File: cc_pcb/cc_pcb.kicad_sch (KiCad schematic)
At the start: 70 parts, among them J1 Conn_02x05_Odd_Even, J10 AC-DC Converter, J2 Wi-Fi Module, J3 Controller (40Pin->SPI), J4 RFID Scanner, J5 4x4 Keypad, J6 SD Reader, J7 PS_Modules, J8 PS_Designed, J9 DC-DC Converter, SW1 SW_Push, U1 STM32F091RCTx, U2 LM393, U3 LD1117S33TR_SOT223

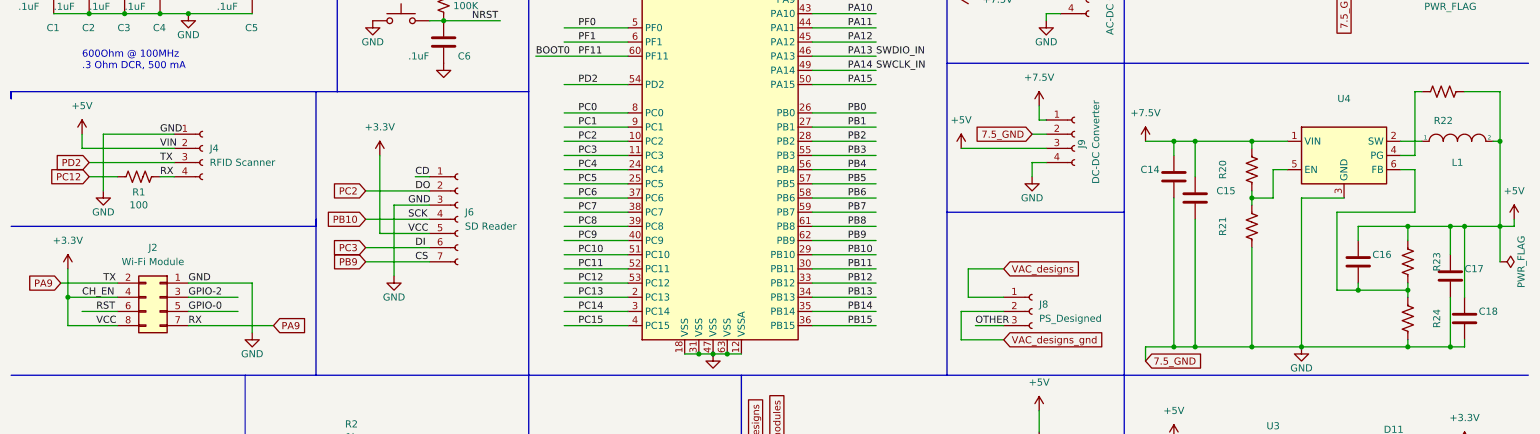
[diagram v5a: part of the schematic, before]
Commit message: RA8875 and ESP8266 updated footprints
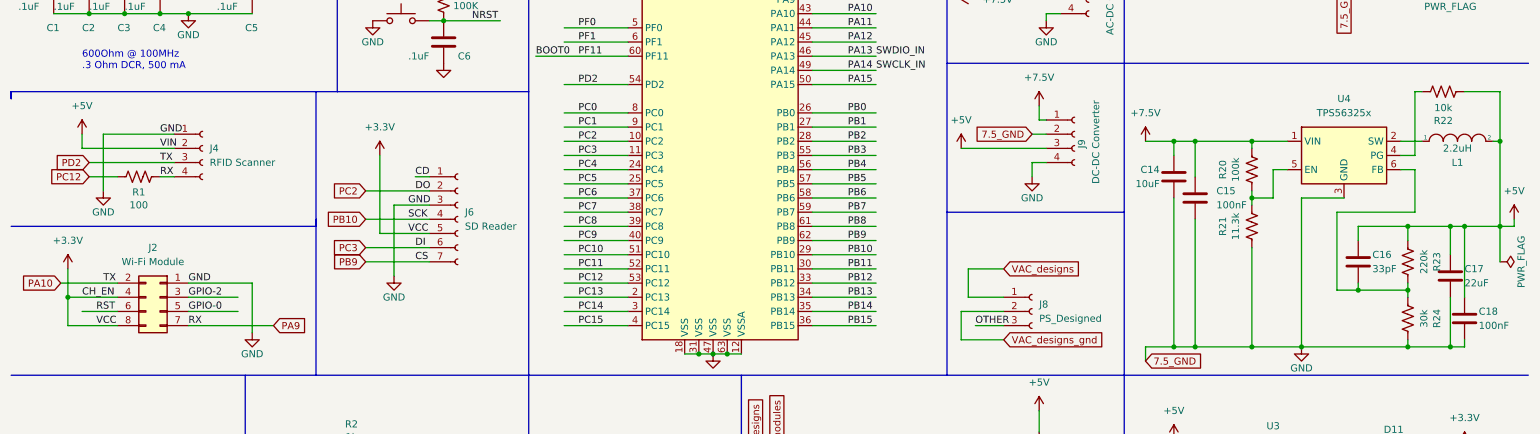
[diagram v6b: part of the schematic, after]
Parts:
- C14: value (none) -> 10uF
- C15, C18: value (none) -> 100nF
- C16: value (none) -> 33pF
- C17: value (none) -> 22uF
- L1: value (none) -> 2.2uH
- R20: value (none) -> 100k
- R21: value (none) -> 11.3k
- R22: value (none) -> 10k
- R23: value (none) -> 220k
- R24: value (none) -> 30k
- U4: value (none) -> TPS56325x
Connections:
- net PA10: now also J2.2 (Pin_2), J4.3 (Pin_3), U1.54 (PD2)
- net PA9: no longer J2.2 (Pin_2), J4.3 (Pin_3), U1.54 (PD2)
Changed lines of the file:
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@@
     )
   )
-  (global_label "PA9" (shape input) (at 21.59 105.41 180) (fields_autoplaced)
+  (global_label "PA10" (shape input) (at 21.59 105.41 180) (fields_autoplaced)
     (effects (font (size 1.27 1.27)) (justify right))
-    (property "Intersheet References" "${INTERSHEET_REFS}" (id 0) (at 15.6088 105.3306 0)
+    (property "Intersheet References" "${INTERSHEET_REFS}" (id 0) (at 14.3993 105.3306 0)
       (effects (font (size 1.27 1.27)) (justify right) hide)
     )
@@
     (in_bom yes) (on_board yes)
     (property "Reference" "R22" (id 0) (at 269.24 76.327 90))
-    (property "Value" "" (id 1) (at 269.24 74.0156 90))
+    (property "Value" "10k" (id 1) (at 269.24 74.0156 90))
     (property "Footprint" "Resistor_SMD:R_0805_2012Metric_Pad1.20x1.40mm_HandSolder" (id 2) (at 269.494 70.104 90)
       (effects (font (size 1.27 1.27)) hide)
@@
     (in_bom yes) (on_board yes)
     (property "Reference" "R24" (id 0) (at 268.097 111.76 90))
-    (property "Value" "" (id 1) (at 265.7856 111.76 90))
+    (property "Value" "30k" (id 1) (at 265.7856 111.76 90))
     (property "Footprint" "Resistor_SMD:R_0805_2012Metric_Pad1.20x1.40mm_HandSolder" (id 2) (at 261.874 111.506 90)
       (effects (font (size 1.27 1.27)) hide)
@@
     (in_bom yes) (on_board yes)
     (property "Reference" "L1" (id 0) (at 271.78 83.82 0))
-    (property "Value" "" (id 1) (at 271.78 81.28 0))
+    (property "Value" "2.2uH" (id 1) (at 271.78 81.28 0))
     (property "Footprint" "Inductor_THT:L_Radial_D7.5mm_P5.00mm_Fastron_07P" (id 2) (at 271.78 80.01 0)
       (effects (font (size 1.27 1.27)) hide)
@@
       (effects (font (size 1.27 1.27)) (justify left))
     )
-    (property "Value" "" (id 1) (at 275.59 113.03 0)
+    (property "Value" "100nF" (id 1) (at 275.59 113.03 0)
       (effects (font (size 1.27 1.27)) (justify left))
     )
@@
     (in_bom yes) (on_board yes)
     (property "Reference" "R21" (id 0) (at 229.743 95.25 90))
-    (property "Value" "" (id 1) (at 232.0544 95.25 90))
+    (property "Value" "11.3k" (id 1) (at 232.0544 95.25 90))
     (property "Footprint" "Resistor_SMD:R_0805_2012Metric_Pad1.20x1.40mm_HandSolder" (id 2) (at 235.966 95.504 90)
       (effects (font (size 1.27 1.27)) hide)
@@
     (in_bom yes) (on_board yes)
     (property "Reference" "R23" (id 0) (at 268.097 101.6 90))
-    (property "Value" "" (id 1) (at 265.7856 101.6 90))
+    (property "Value" "220k" (id 1) (at 265.7856 101.6 90))
     (property "Footprint" "Resistor_SMD:R_0805_2012Metric_Pad1.20x1.40mm_HandSolder" (id 2) (at 261.874 101.346 90)
       (effects (font (size 1.27 1.27)) hide)
@@
       (effects (font (size 1.27 1.27)) (justify left))
     )
-    (property "Value" "" (id 1) (at 228.6 91.44 0)
+    (property "Value" "100nF" (id 1) (at 228.6 91.44 0)
       (effects (font (size 1.27 1.27)) (justify left))
     )
@@
       (effects (font (size 1.27 1.27)) (justify left))
     )
-    (property "Value" "" (id 1) (at 218.44 87.63 0)
+    (property "Value" "10uF" (id 1) (at 218.44 87.63 0)
       (effects (font (size 1.27 1.27)) (justify left))
     )
@@
     (in_bom yes) (on_board yes)
     (property "Reference" "R20" (id 0) (at 229.743 85.09 90))
-    (property "Value" "" (id 1) (at 232.0544 85.09 90))
+    (property "Value" "100k" (id 1) (at 232.0544 85.09 90))
     (property "Footprint" "Resistor_SMD:R_0805_2012Metric_Pad1.20x1.40mm_HandSolder" (id 2) (at 235.966 85.344 90)
       (effects (font (size 1.27 1.27)) hide)
@@
       (effects (font (size 1.27 1.27)) (justify left))
     )
-    (property "Value" "" (id 1) (at 256.54 102.87 0)
+    (property "Value" "33pF" (id 1) (at 256.54 102.87 0)
       (effects (font (size 1.27 1.27)) (justify left))
     )
@@
       (effects (font (size 1.27 1.27)) (justify left))
     )
-    (property "Value" "" (id 1) (at 273.05 105.41 0)
+    (property "Value" "22uF" (id 1) (at 273.05 105.41 0)
       (effects (font (size 1.27 1.27)) (justify left))
     )
@@
     (in_bom yes) (on_board yes) (fields_autoplaced)
     (property "Reference" "U4" (id 0) (at 251.46 72.39 0))
-    (property "Value" "" (id 1) (at 251.46 74.93 0))
+    (property "Value" "TPS56325x" (id 1) (at 251.46 74.93 0))
     (property "Footprint" "" (id 2) (at 252.73 88.9 0)
       (effects (font (size 1.27 1.27)) (justify left) hide)

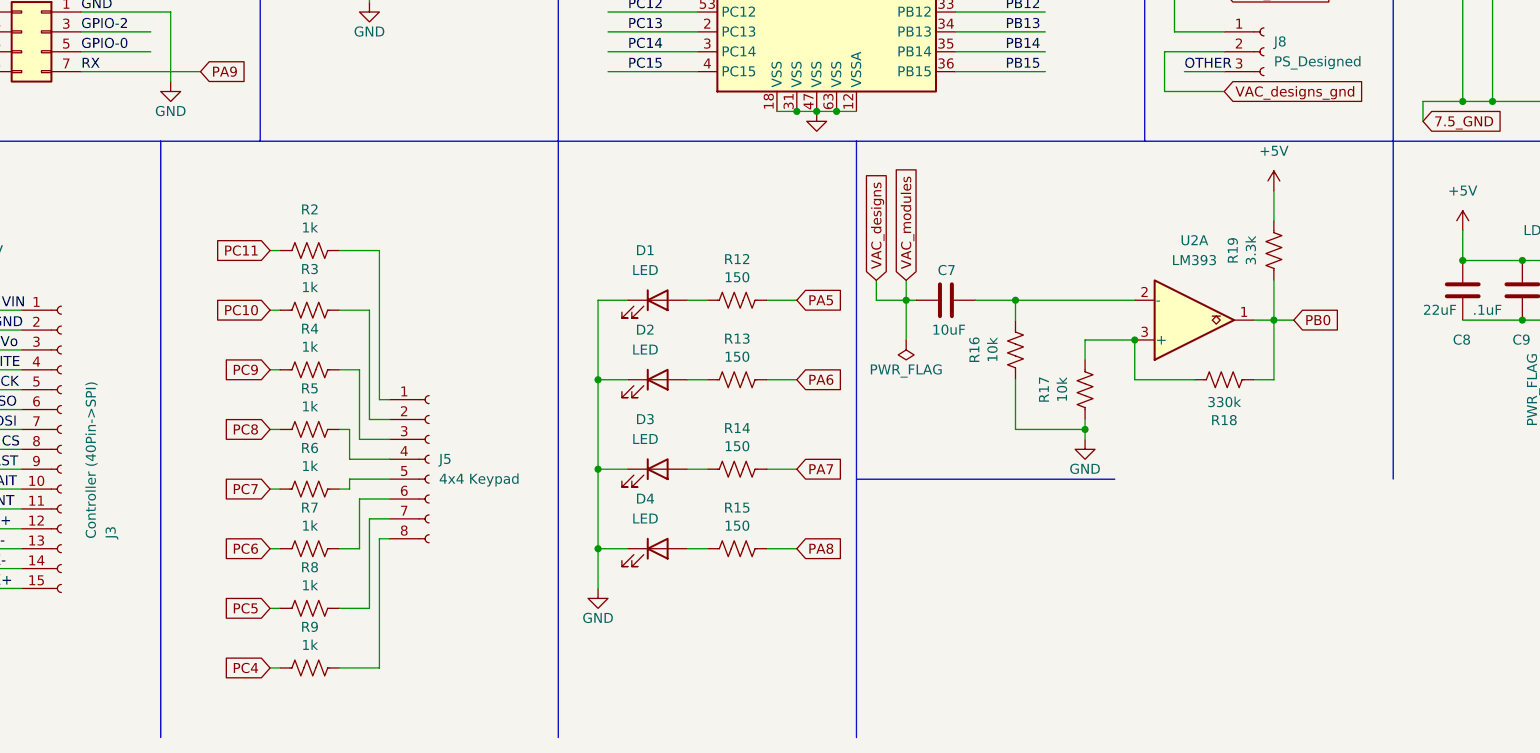
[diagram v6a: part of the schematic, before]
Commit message: added 2.8in tft display in addition to 7in one
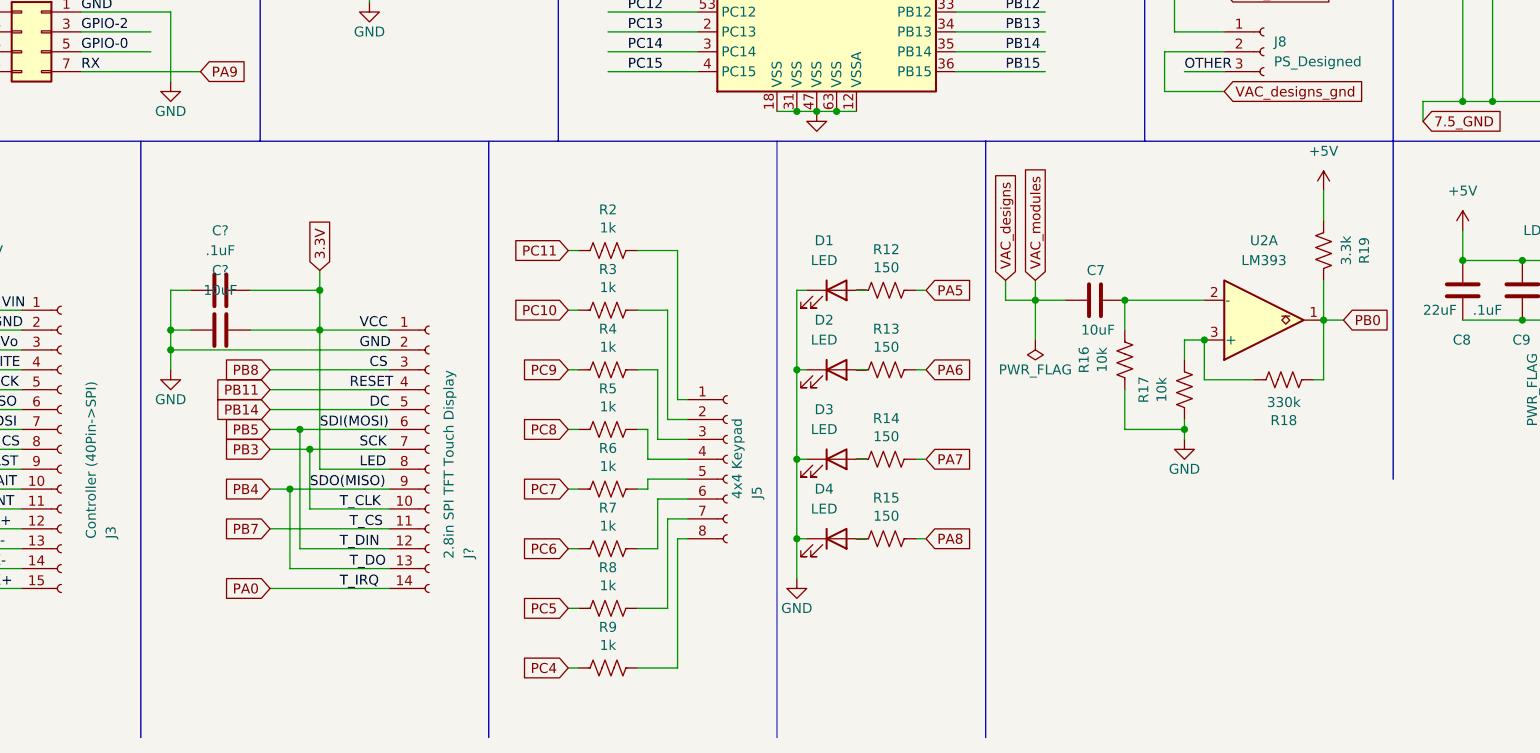
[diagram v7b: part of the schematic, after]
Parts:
- added C?: 10uF, symbol Device:C
- added C?: .1uF, symbol Device:C
- added J?: 2.8in SPI TFT Touch Display, symbol Connector:Conn_01x14_Female
- U4: footprint (none) -> imported_footprints:TPS56325x
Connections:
- net PB4 is gone; now on net PB10: J3.6 (Pin_6), U1.56 (PB4)
- net PB5 is gone; now on net +3V3: J3.7 (Pin_7), U1.57 (PB5)
- net +3V3: now also C?.2, C?.2, J?.1 (Pin_1), J?.12 (Pin_12), J?.6 (Pin_6), J?.8 (Pin_8)
- net GND: now also C?.1, C?.1, J?.2 (Pin_2)
- net PA0: now also J?.14 (Pin_14)
- net PB10: now also J?.10 (Pin_10), J?.13 (Pin_13), J?.7 (Pin_7), J?.9 (Pin_9)
- net PB11: now also J?.4 (Pin_4)
- net PB14: now also J?.5 (Pin_5)
- net PB7: now also J?.11 (Pin_11)
- net PB8: now also J?.3 (Pin_3)
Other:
- moved on the sheet: C7, D1, D2, D3, D4, J5, R12, R13, R14, R15, R16, R17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

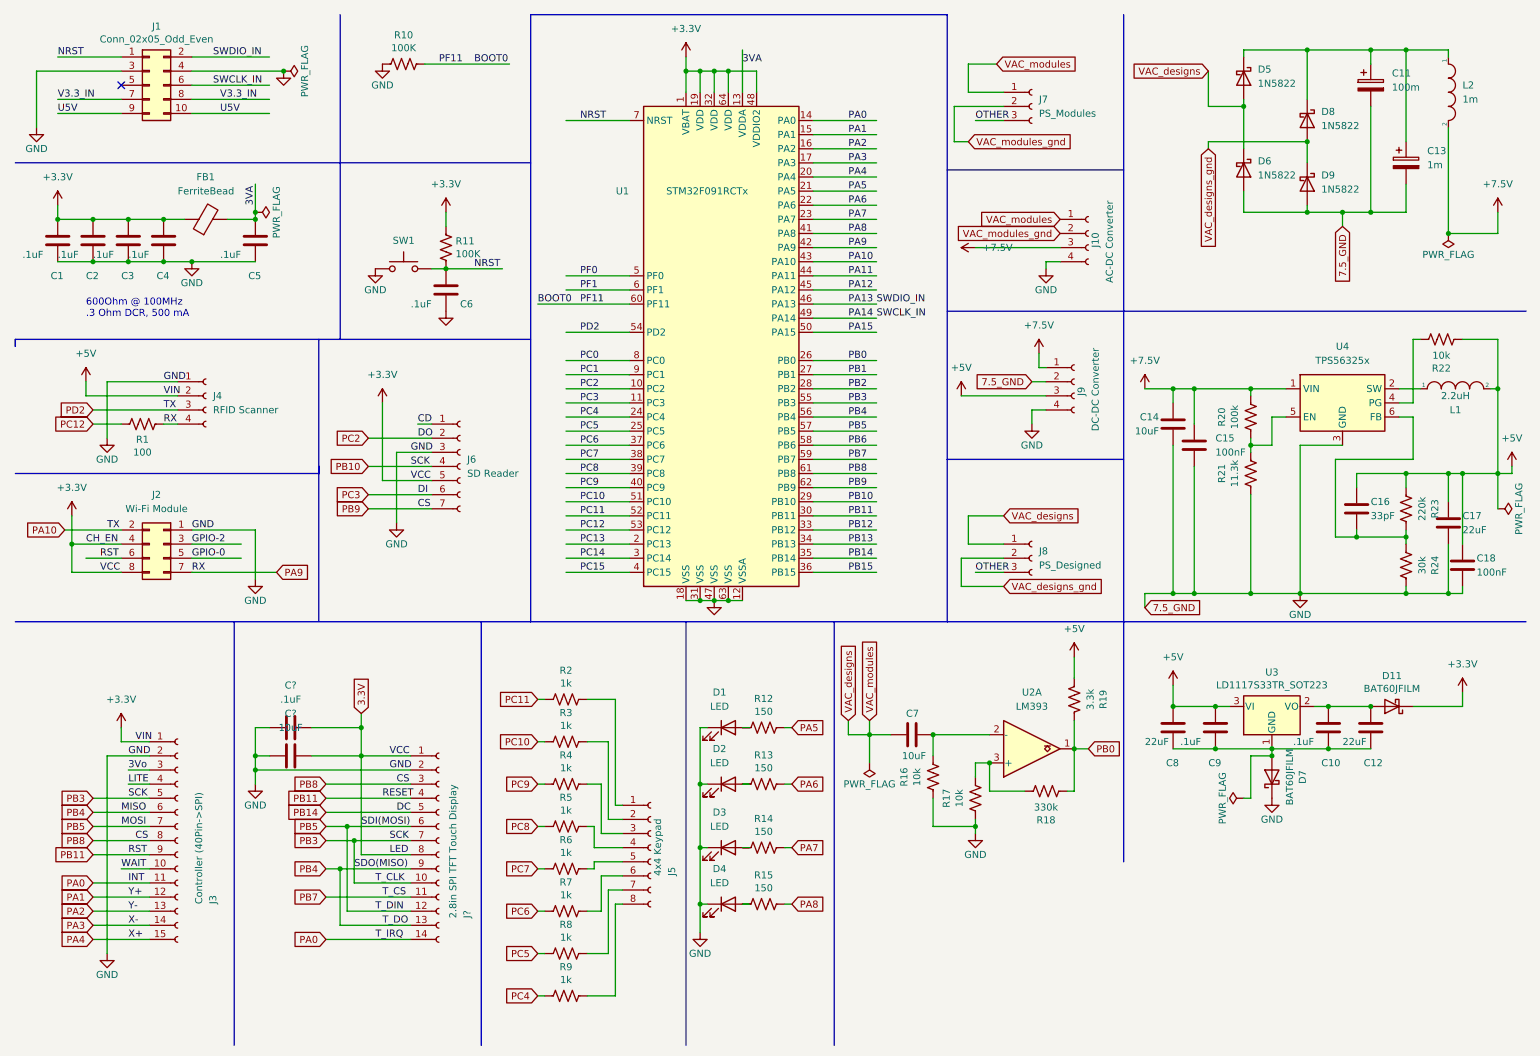
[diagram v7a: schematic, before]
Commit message: micro sd connector schematic/footprint, lm324 footprint
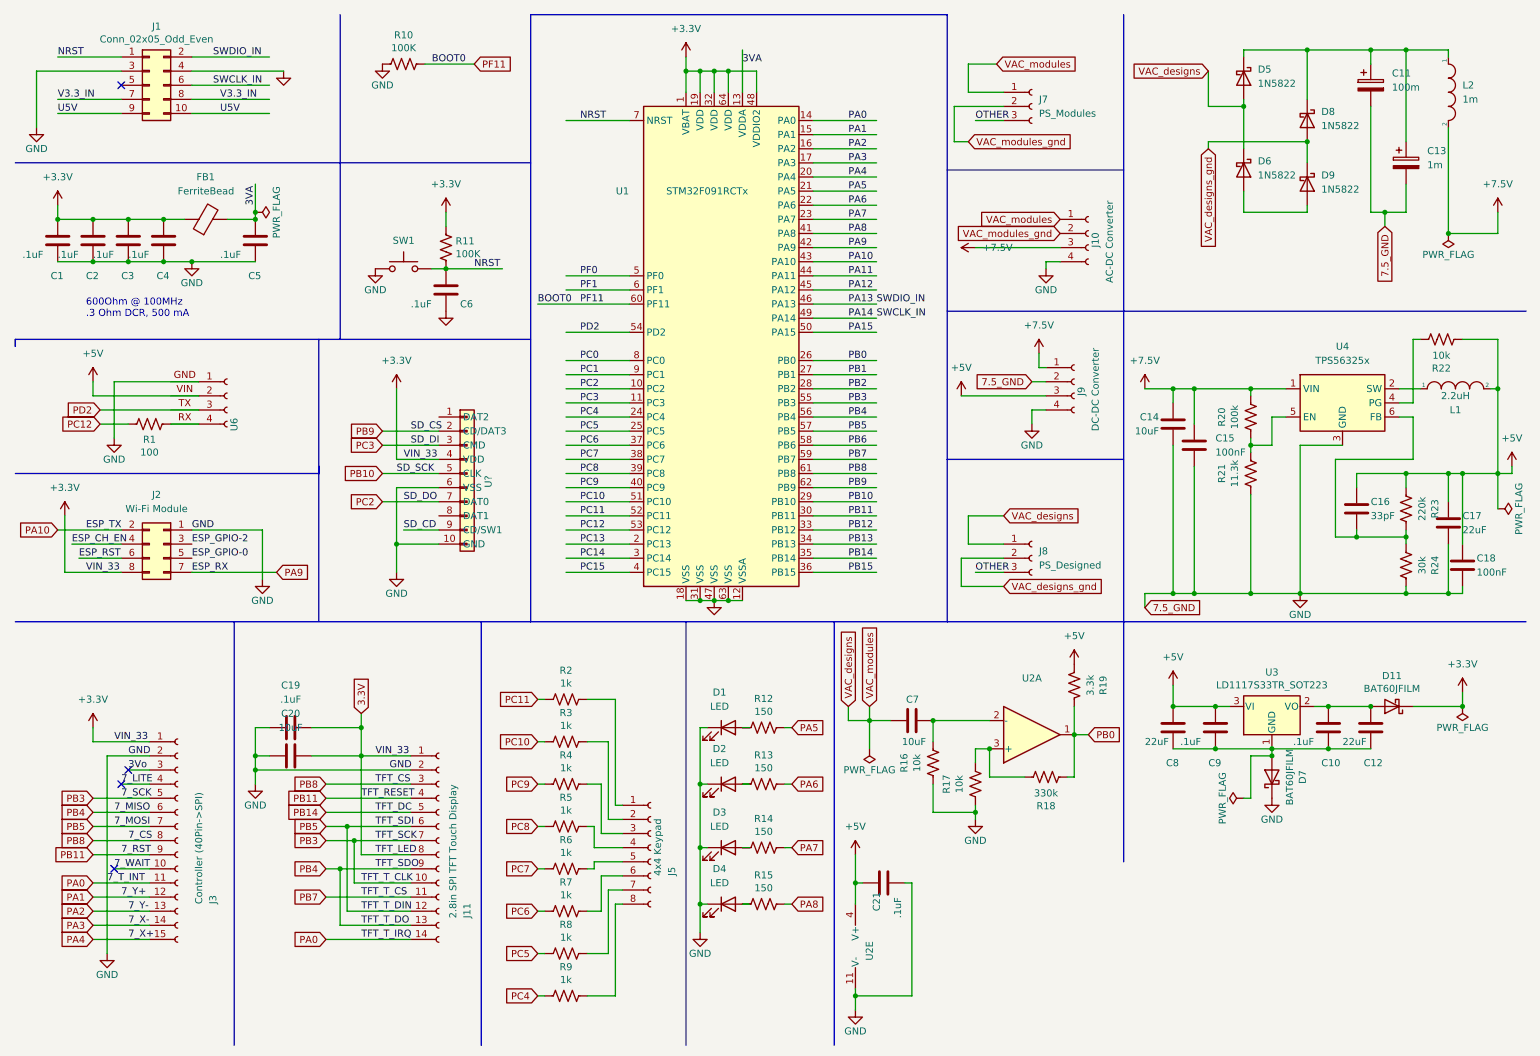
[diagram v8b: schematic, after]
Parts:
- removed J4: RFID Scanner, imported_footprints:RFID_Reader_PCB, symbol Connector:Conn_01x04_Female
- removed J6: SD Reader, imported_footprints:Micro_SD_card_reader, symbol Connector:Conn_01x07_Female
- removed U2: LM393, imported_footprints:LM393, symbol Comparator:LM393
- added C21: .1uF, Capacitor_SMD:C_0805_2012Metric_Pad1.18x1.45mm_HandSolder, symbol Device:C
- added U2: (no value), symbol Amplifier_Operational:LM324
- added U6: (no value), symbol created_schematics:RFID_Scanner
- added U?: (no value), symbol created_schematics:wurth_SD
- C5: footprint Capacitor_SMD:C_0805_2012Metric_Pad1.18x1.45mm_HandSolder -> (none)
- FB1: footprint Ferrite_THT:LairdTech_28C0236-0JW-10 -> (none)
- J11: renamed from J?; footprint (none) -> imported_footprints:tft_2.8in_touch_display
- J3: footprint imported_footprints:RA8875_TFT_Breakout -> (none)
- gave numbers to parts that had none: 2
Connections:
- net PA0 is gone; now on net GND: J11.14 (Pin_14), J3.11 (Pin_11), U1.14 (PA0)
- net +3V3: now also J11.4 (Pin_4), J3.9 (Pin_9), U1.30 (PB11), U?.4 (VDD); no longer C16.1, C17.1, C18.1, C8.1, C9.1, J11.12 (Pin_12), J11.6 (Pin_6), J2.4 (Pin_4), J3.7 (Pin_7), J9.3 (Pin_3), L1.2, R19.1, R22.2, R23.2, U1.57 (PB5), U3.3 (VI)
- net GND: now also C21.2, U2.11 (V-), U6.1, U?.10 (GND), U?.6 (VSS); no longer D6.2 (A), D9.2 (A)
- net PA10: no longer U1.54 (PD2)
- net PA9: no longer R1.1
- net PB0: now also U2.1
- net PB10: now also U?.5 (CLK); no longer J11.10 (Pin_10), J11.13 (Pin_13), J11.7 (Pin_7), J11.9 (Pin_9), J3.5 (Pin_5), J3.6 (Pin_6), U1.55 (PB3), U1.56 (PB4)
- net PB8: no longer U1.62 (PB9)
- net PC2: now also U?.7 (DAT0)
- net PC3: now also U?.3 (CMD)
- net at C7.2, R16.1: now also U2.2 (-)
- net at R17.1, R18.1: now also U2.3 (+)
- net BOOT0 renamed PF11
- net GPIO-0 renamed ESP_GPIO-0
- net GPIO-2 renamed ESP_GPIO-2
- net LITE renamed 7_LITE
- removed net PB11: J11.4 (Pin_4), J2.6 (Pin_6), J3.9 (Pin_9), U1.30 (PB11)
- net WAIT renamed 7_WAIT
- new net: D6.2 (A), D9.2 (A)
- new net: R1.1, U6.4
- new net +5V: C16.1, C17.1, C18.1, C21.1, C8.1, C9.1, J9.3 (Pin_3), L1.2, R19.1, R22.2, R23.2, U2.4 (V+), U3.3 (VI), U6.2
- new net ESP_CH_EN: J2.4 (Pin_4)
- new net ESP_RST: J2.6 (Pin_6)
- new net PB3: J11.10 (Pin_10), J11.7 (Pin_7), J3.5 (Pin_5), U1.55 (PB3)
- new net PB4: J11.13 (Pin_13), J11.9 (Pin_9), J3.6 (Pin_6), U1.56 (PB4)
- new net PB5: J11.12 (Pin_12), J11.6 (Pin_6), J3.7 (Pin_7), U1.57 (PB5)
- new net PB9: U1.62 (PB9), U?.2 (CD/DAT3)
- new net PD2: U1.54 (PD2), U6.3
- new net SD_CD: U?.9 (CD/SW1)
- no-connect marks 1 -> 4
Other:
- moved on the sheet: C7, R1, R16, R17, R18, R19
